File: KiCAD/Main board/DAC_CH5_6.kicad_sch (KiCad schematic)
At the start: 43 parts, among them U1 PCM1789, U3 OPA1632DR, U4 OPA1632DR

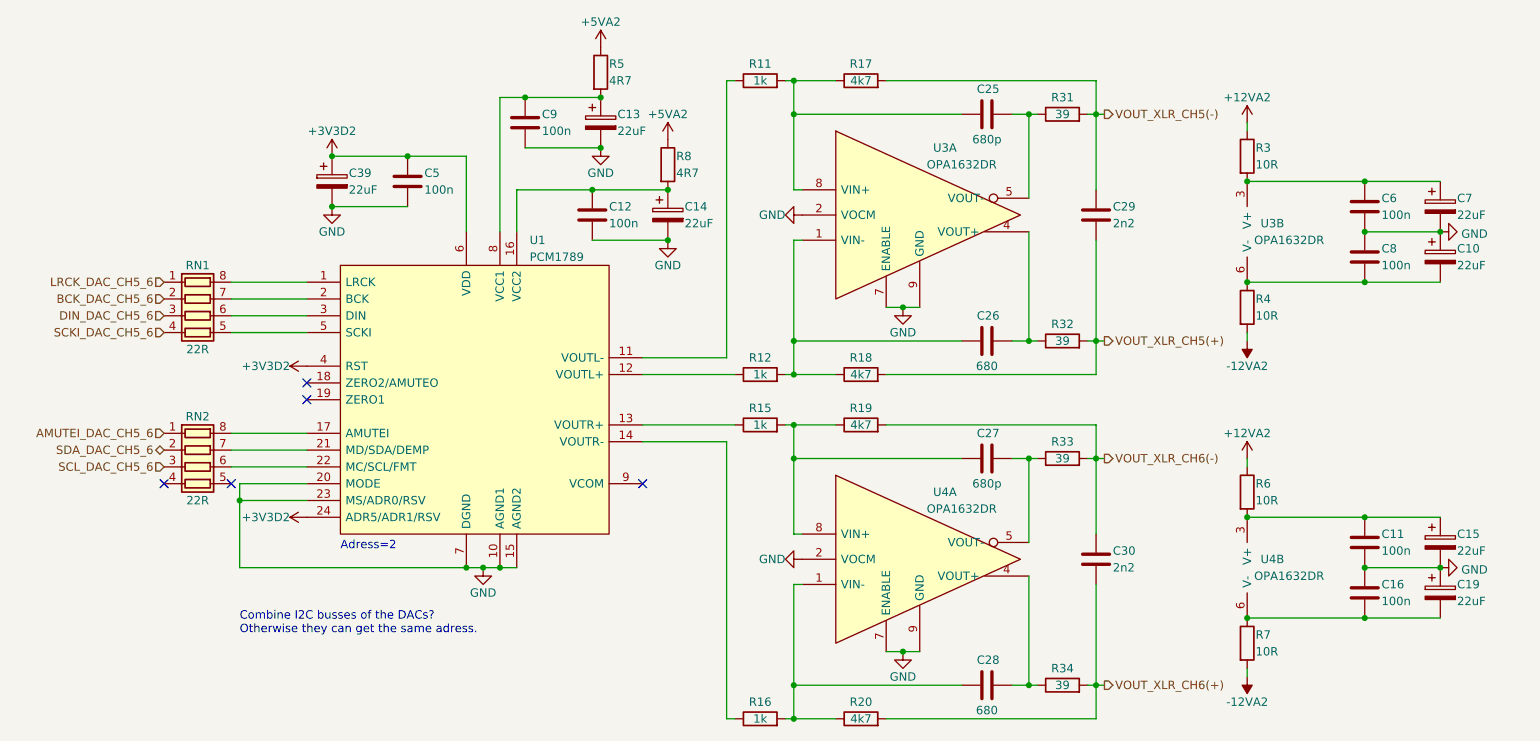
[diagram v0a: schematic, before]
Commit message: Finalizer main board schematic exept passive order links. Schematic ready for review
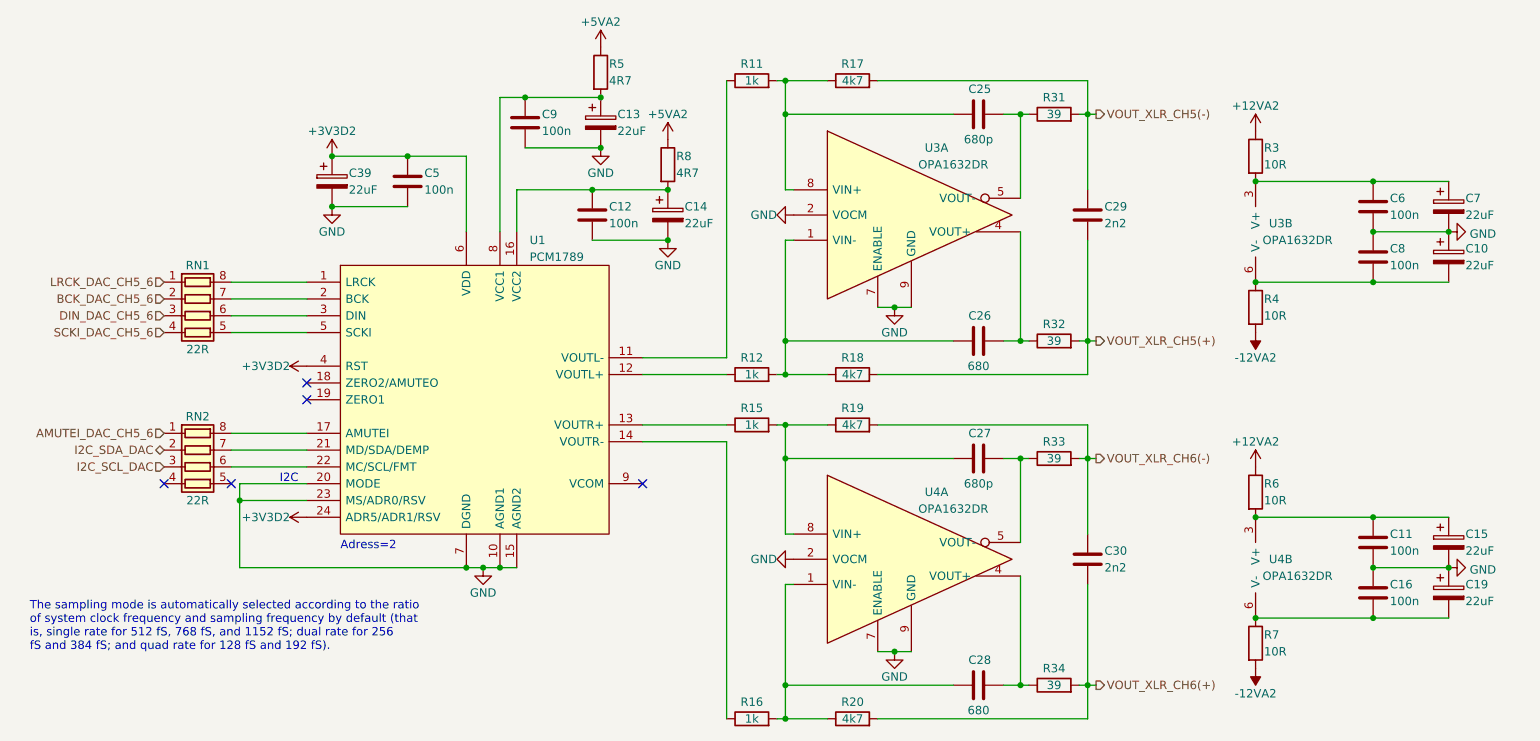
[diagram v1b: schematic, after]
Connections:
- net SCL_DAC_CH5_6 renamed I2C_SCL_DAC
- net SDA_DAC_CH5_6 renamed I2C_SDA_DAC
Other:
- note added: "I2C"
- note added: "The sampling mode is automatically selected according to the ratio of system clock frequency and sampling frequency by default (that is, single rate for 512 fS, 768 fS, and 1152 fS; dual rate for 256 fS and 384 fS; and quad rate for 128 fS and 192 fS)."
- note removed: "Combine I2C busses of the DACs? Otherwise they can get the same adress."
- moved on the sheet: C10, C11, C15, C16, C19, C25, C26, C27, C28, C29, C30, C6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

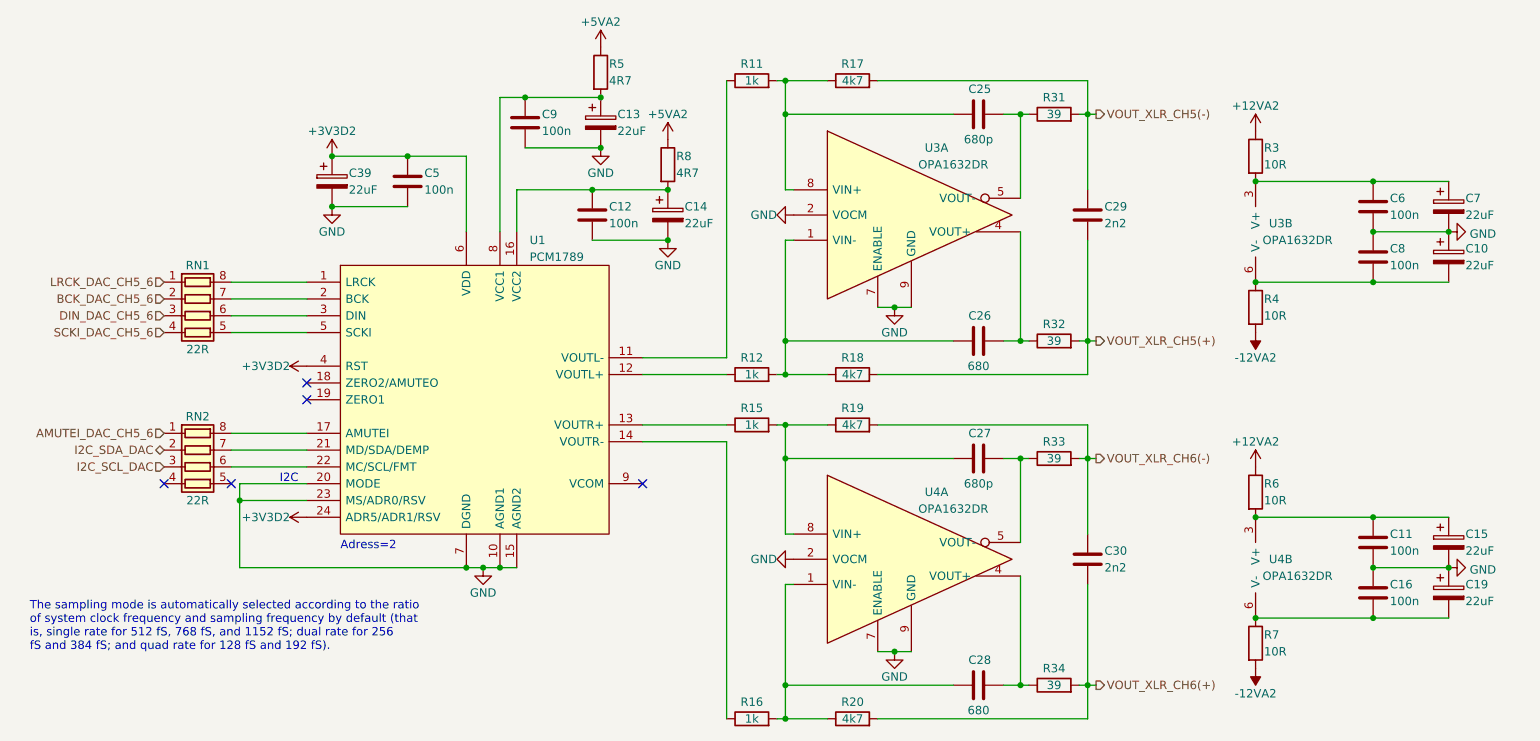
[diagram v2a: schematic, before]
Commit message: Added component links
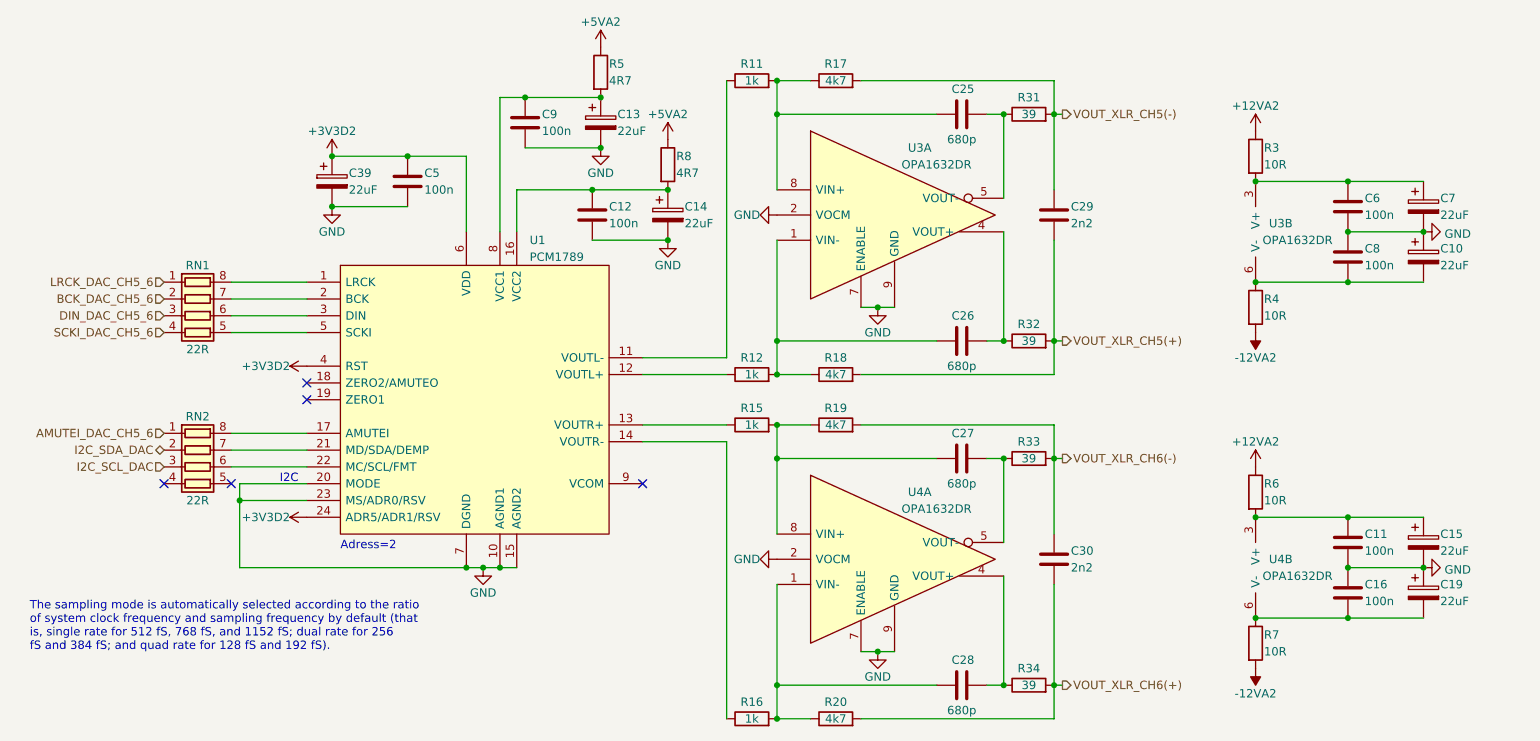
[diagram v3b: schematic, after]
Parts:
- C26, C28: value 680 -> 680p
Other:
- moved on the sheet: C10, C11, C15, C16, C19, C25, C26, C27, C28, C29, C30, C6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

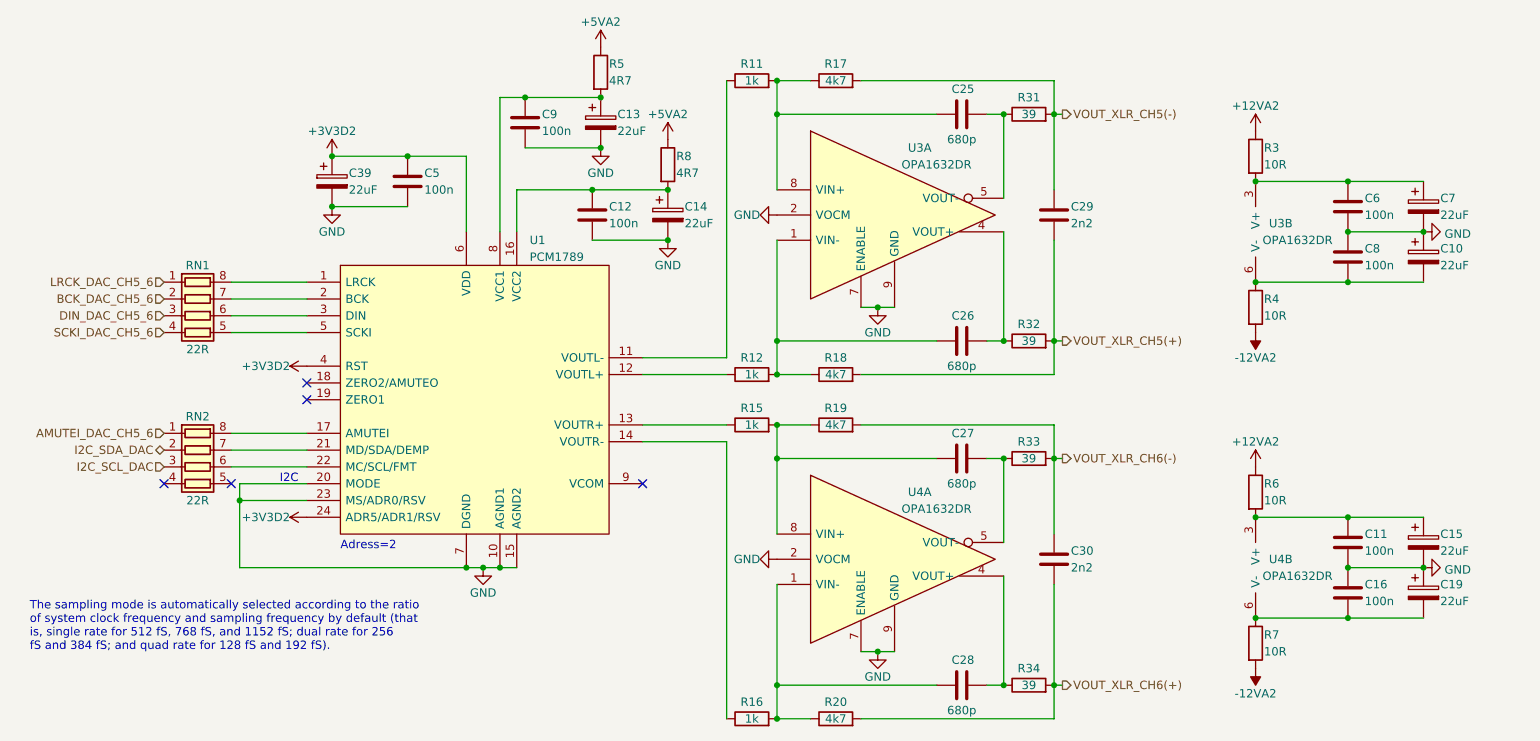
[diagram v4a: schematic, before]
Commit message: Added rotary encoder and pull-up
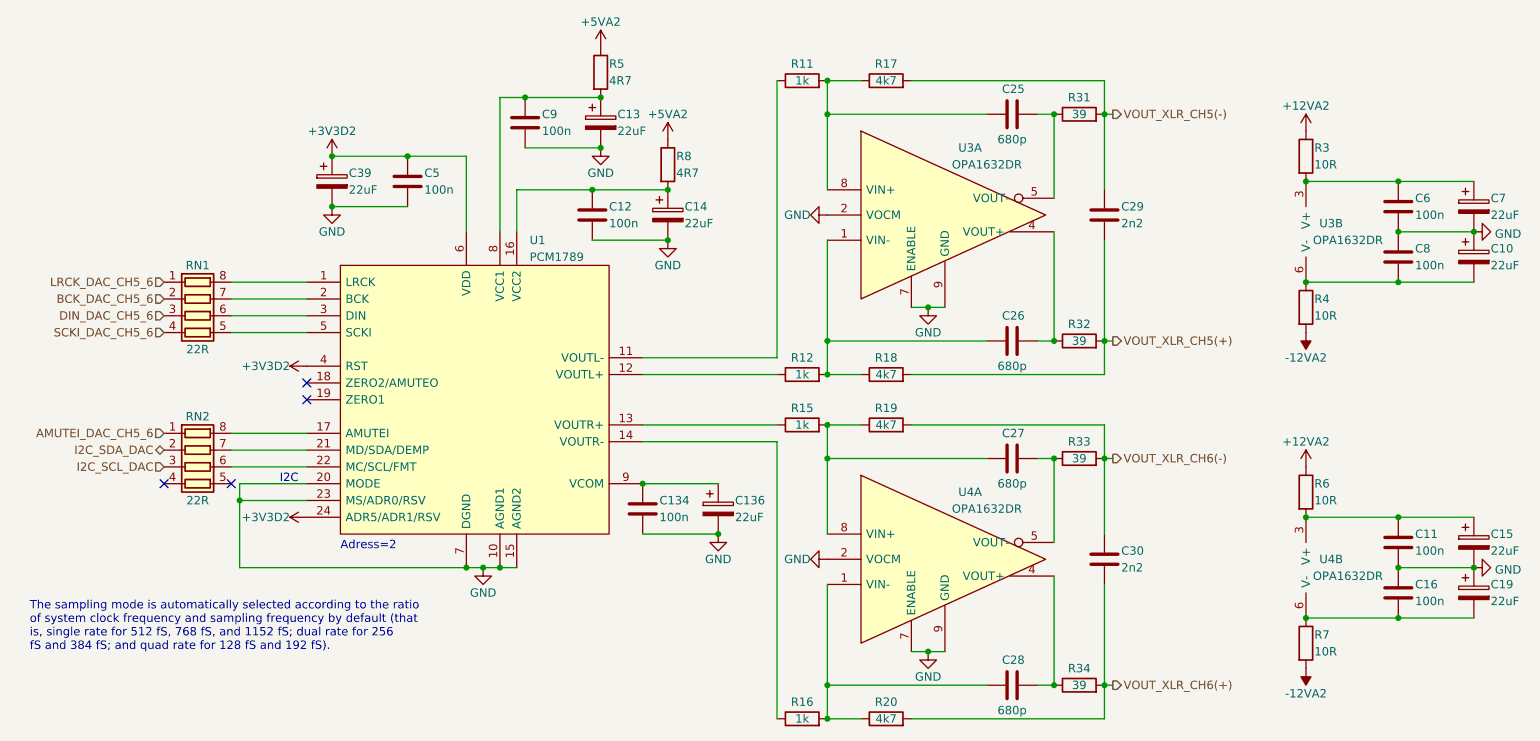
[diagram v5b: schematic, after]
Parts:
- added C134: 100n, Capacitor_SMD:C_0402_1005Metric, symbol Device:C
- added C136: 22uF, Capacitor_THT:CP_Radial_D5.0mm_P2.00mm, symbol Device:C_Polarized
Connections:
- net GND: now also C134.2, C136.2
- net at U1.9 (VCOM): now also C134.1, C136.1
- no-connect marks 5 -> 4
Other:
- moved on the sheet: C10, C11, C15, C16, C19, C25, C26, C27, C28, C29, C30, C6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
